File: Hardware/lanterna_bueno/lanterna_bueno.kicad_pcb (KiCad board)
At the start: 2 copper layers, 50 parts, among them J1 USB_B_Micro, Q1 BC807, Q2 2SK4075, Q3 2SK4075, Q4 2SK4075, Q5 2SK4075, SW1 SW_Push, SW2 SW_Push, SW3 SW_Push, U1 RT9193-33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

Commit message: add Mechanical DXF
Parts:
- moved DS1 67.9 mm to (88.9, 106.7)
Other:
- board outline added: 190.3 x 82.2 mm

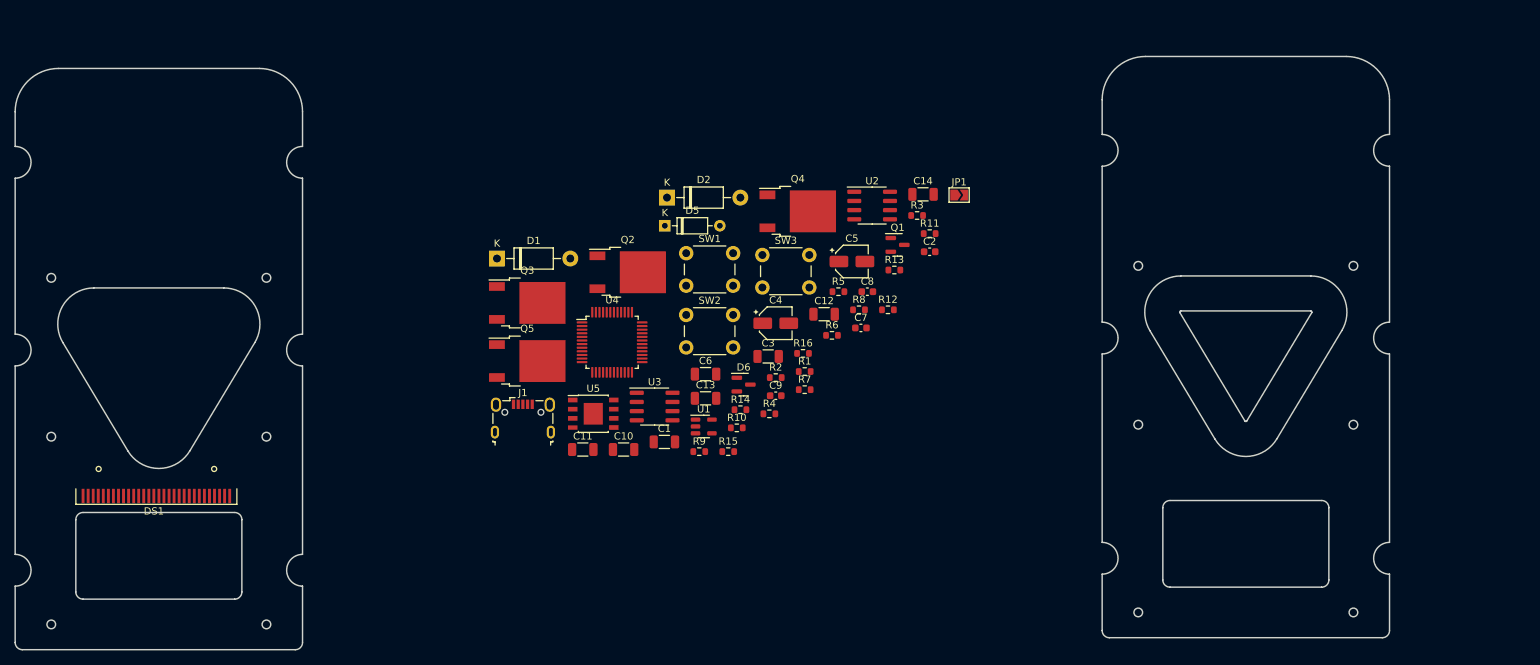
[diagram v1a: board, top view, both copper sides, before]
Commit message: Starting board, mounting holes OK
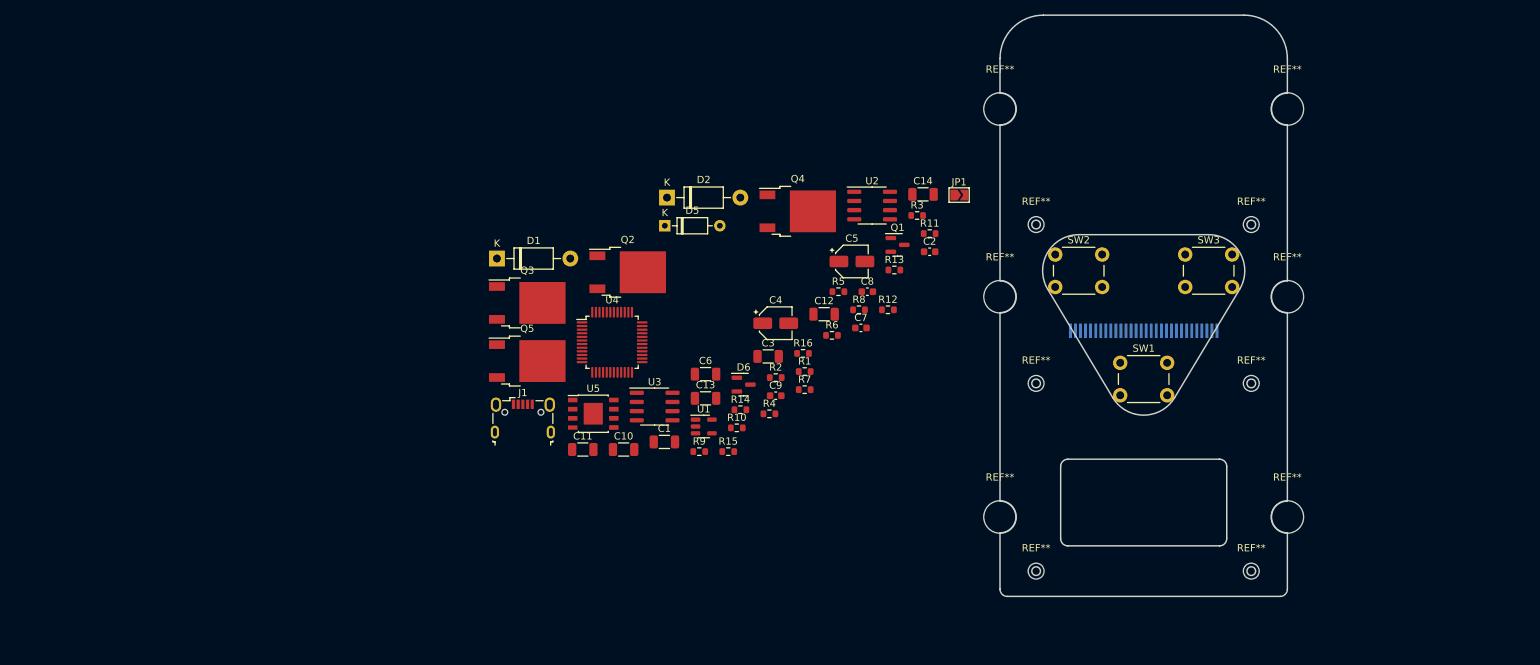
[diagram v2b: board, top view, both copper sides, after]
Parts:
- added REF**: MountingHole_2.2mm_M2, MountingHole:MountingHole_2.2mm_M2, F.Cu at (240.5, 69.1)
- added REF**: MountingHole_4.5mm, MountingHole:MountingHole_4.5mm, F.Cu at (205.7, 53.1)
- added REF**: MountingHole_2.2mm_M2, MountingHole:MountingHole_2.2mm_M2, F.Cu at (210.7, 117.1)
- added REF**: MountingHole_2.2mm_M2, MountingHole:MountingHole_2.2mm_M2, F.Cu at (240.5, 91.1)
- added REF**: MountingHole_4.5mm, MountingHole:MountingHole_4.5mm, F.Cu at (245.5, 53.1)
- added REF**: MountingHole_4.5mm, MountingHole:MountingHole_4.5mm, F.Cu at (205.7, 79.1)
- added REF**: MountingHole_2.2mm_M2, MountingHole:MountingHole_2.2mm_M2, F.Cu at (210.7, 69.1)
- added REF**: MountingHole_4.5mm, MountingHole:MountingHole_4.5mm, F.Cu at (205.7, 109.6)
- added REF**: MountingHole_2.2mm_M2, MountingHole:MountingHole_2.2mm_M2, F.Cu at (210.7, 91.1)
- added REF**: MountingHole_2.2mm_M2, MountingHole:MountingHole_2.2mm_M2, F.Cu at (240.5, 117.1)
- added REF**: MountingHole_4.5mm, MountingHole:MountingHole_4.5mm, F.Cu at (245.5, 109.6)
- added REF**: MountingHole_4.5mm, MountingHole:MountingHole_4.5mm, F.Cu at (245.5, 79.1)
- DS1: moved to B.Cu
- moved DS1 138.6 mm to (225.6, 83.8)
- moved SW1 62.0 mm to (222.4, 88.2)
- moved SW3 58.6 mm to (231.4, 73.2)
- moved SW2 51.8 mm to (213.4, 73.2)
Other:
- board size 190.3 x 82.2 mm -> 39.8 x 80.5 mm

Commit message: Flat do Oled posicionado
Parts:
- BTN +: renamed from SW2
- BTN -: renamed from SW3
- BTN M: renamed from SW1
- JP1, U4: moved to B.Cu
- moved U4 76.3 mm to (225.3, 64.0), turned to -45 degrees
- moved JP1 20.6 mm to (218.9, 56.6), turned to 45 degrees
- moved DS1 17.8 mm to (225.7, 101.6)
- moved BTN - 7.93 mm to (237.9, 77.7), turned to 180 degrees
- moved BTN + 7.90 mm to (219.9, 77.7), turned to 180 degrees
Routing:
- added copper zone on B.Cu, net GND
- added copper zone on F.Cu, net GND
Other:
- outline, holes or cut-outs redrawn

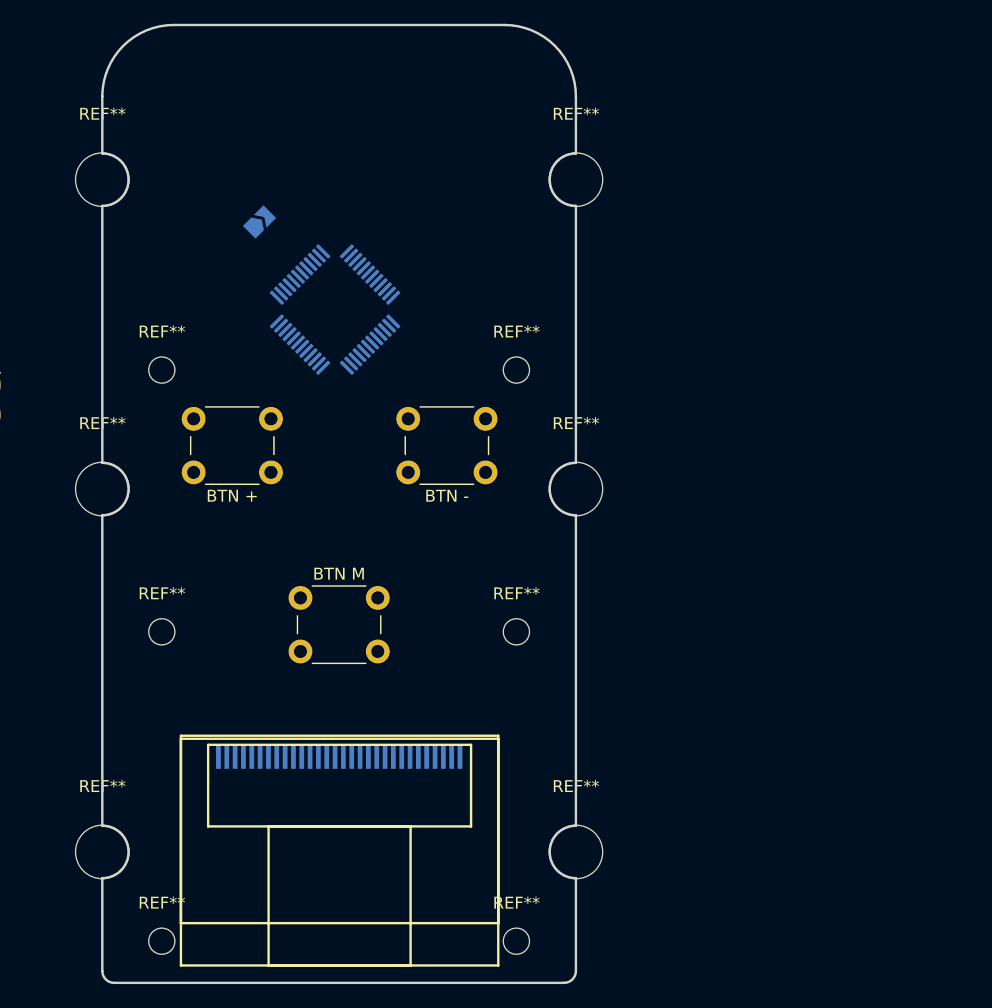
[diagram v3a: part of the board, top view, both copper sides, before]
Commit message: Adicionado PCB Carga e Board Profile corrigido
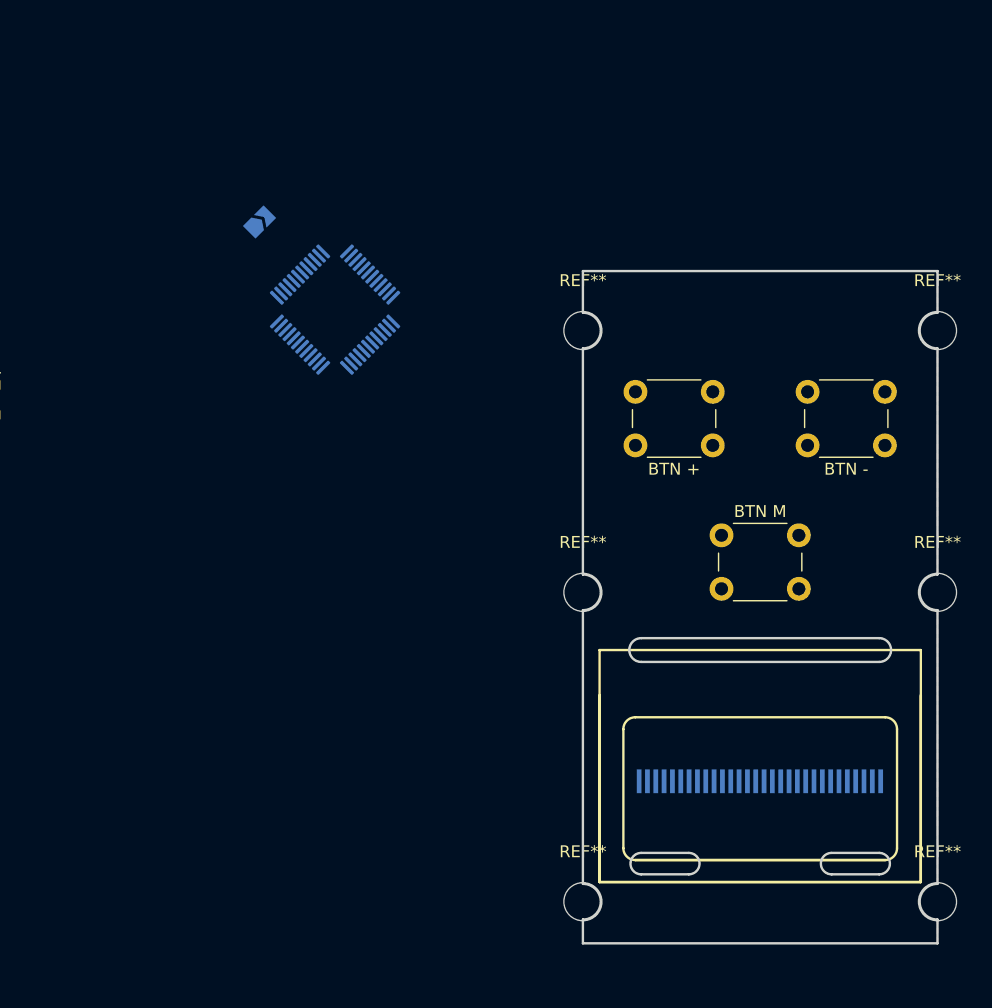
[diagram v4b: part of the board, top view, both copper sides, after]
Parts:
- removed the REF** at (240.5, 69.1)
- removed the REF** at (205.7, 53.1)
- removed the REF** at (210.7, 117.1)
- removed the REF** at (240.5, 91.1)
- removed the REF** at (245.5, 53.1)
- removed the REF** at (205.7, 79.1)
- removed the REF** at (210.7, 69.1)
- removed the REF** at (205.7, 109.6)
- removed the REF** at (210.7, 91.1)
- removed the REF** at (240.5, 117.1)
- removed the REF** at (245.5, 109.6)
- removed the REF** at (245.5, 79.1)
- added REF**: MountingHole_3.2mm_M3, MountingHole:MountingHole_3.2mm_M3, F.Cu at (246.1, 87.8)
- added REF**: MountingHole_3.2mm_M3, MountingHole:MountingHole_3.2mm_M3, F.Cu at (275.9, 113.8)
- added REF**: MountingHole_3.2mm_M3, MountingHole:MountingHole_3.2mm_M3, F.Cu at (246.1, 113.8)
- added REF**: MountingHole_3.2mm_M3, MountingHole:MountingHole_3.2mm_M3, F.Cu at (275.9, 87.8)
- added REF**: MountingHole_3.2mm_M3, MountingHole:MountingHole_3.2mm_M3, F.Cu at (246.1, 65.8)
- added REF**: MountingHole_3.2mm_M3, MountingHole:MountingHole_3.2mm_M3, F.Cu at (275.9, 65.8)
- moved BTN + 37.2 mm to (257.0, 75.4)
- moved BTN M 35.8 mm to (257.8, 83.0)
- moved DS1 35.4 mm to (261.0, 103.6), turned to 180 degrees
- moved BTN - 33.6 mm to (271.5, 75.4)
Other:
- board size 39.8 x 80.5 mm -> 29.8 x 56.5 mm

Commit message: building
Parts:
- removed C10: 1uF, Capacitor_SMD:C_1206_3216Metric
- removed C7: 100nF, Capacitor_SMD:C_0603_1608Metric
- removed D6: BAT54C, Package_TO_SOT_SMD:SOT-23
- removed JP1: SolderJumper_2_Open, Jumper:SolderJumper-2_P1.3mm_Open_TrianglePad1.0x1.5mm
- removed R8: 47K, Resistor_SMD:R_0603_1608Metric
- C12, C13: footprint Capacitor_SMD:C_1206_3216Metric -> Capacitor_SMD:C_0603_1608Metric
- D1, D2: footprint Diode_THT:D_DO-41_SOD81_P10.16mm_Horizontal -> Diode_SMD:D_SMA
- D5: footprint Diode_THT:D_DO-35_SOD27_P7.62mm_Horizontal -> Diode_SMD:D_SOD-123
- SW1: renamed from BTN M; footprint Button_Switch_THT:SW_PUSH_6mm -> Button_Switch_SMD:SW_Push_1P1T_NO_6x6mm_H9.5mm
- SW2: renamed from BTN +; footprint Button_Switch_THT:SW_PUSH_6mm -> Button_Switch_SMD:SW_Push_1P1T_NO_6x6mm_H9.5mm
- SW3: renamed from BTN -; footprint Button_Switch_THT:SW_PUSH_6mm -> Button_Switch_SMD:SW_Push_1P1T_NO_6x6mm_H9.5mm
- U2: moved to B.Cu
- U4: value STM32F103CBTx -> STM32F042K6Tx; footprint Package_QFP:LQFP-48_7x7mm_P0.5mm -> Package_QFP:LQFP-32_7x7mm_P0.8mm
- moved SW3 76.8 mm to (194.8, 80.6)
- moved SW2 76.8 mm to (180.4, 80.5)
- moved REF** 73.8 mm to (202.5, 121.1)
- moved REF** 73.8 mm to (202.5, 95.1)
- moved REF** 73.8 mm to (202.5, 73.1)
- moved DS1 73.8 mm to (187.6, 111.0)
- moved REF** 73.8 mm to (172.7, 95.1)
- moved REF** 73.8 mm to (172.7, 121.1)
- moved REF** 73.8 mm to (172.7, 73.1)
- moved SW1 70.8 mm to (187.6, 92.6)
- moved D5 53.3 mm to (189.7, 113.0), turned to 180 degrees
- moved Q4 50.4 mm to (148.0, 107.9), turned to -90 degrees
- moved U5 47.9 mm to (197.3, 93.4), turned to 90 degrees
- moved C14 45.7 mm to (181.0, 108.4)
- moved C11 44.4 mm to (189.7, 115.3)
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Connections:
- U4 pad 1: VBAT -> +3V3
- U4 pad 10: BAT_MON -> unconnected-(U4-Pad10)
- U4 pad 12: unconnected-(U4-Pad12) -> PWM_LED_SUPH
- U4 pad 13: unconnected-(U4-Pad13) -> PWM_LED_SUPL
- U4 pad 14: unconnected-(U4-Pad14) -> PWM_LED_INFH
- U4 pad 15: unconnected-(U4-Pad15) -> PWM_LED_INFL
- U4 pad 16: PWM_LED_SUPH -> GND
- U4 pad 17: PWM_LED_SUPL -> +3V3
- U4 pad 18: PWM_LED_INFH -> unconnected-(U4-Pad18)
- U4 pad 19: PWM_LED_INFL -> unconnected-(U4-Pad19)
- U4 pad 2: unconnected-(U4-Pad2) -> LCD_SDA
- U4 pad 23: GND -> unconnected-(U4-Pad23)
- U4 pad 24: +3V3 -> unconnected-(U4-Pad24)
- U4 pad 25: BUT_MINUS -> unconnected-(U4-Pad25)
- U4 pad 26: BUT_PLUS -> BUT_MINUS
- U4 pad 27: BUT_MENU -> BUT_PLUS
- U4 pad 28: POWER_CMD -> BUT_MENU
- U4 pad 29: unconnected-(U4-Pad29) -> POWER_CMD
- U4 pad 3: unconnected-(U4-Pad3) -> LCD_SCL
- U4 pad 32: unconnected-(U4-Pad32) -> GND
- U4 pad 4: unconnected-(U4-Pad4) -> Net-(R9-Pad2)
- U4 pad 5: unconnected-(U4-Pad5) -> +3V3
- U4 pad 6: unconnected-(U4-Pad6) -> BAT_MON
- U4 pad 7: Net-(R9-Pad2) -> unconnected-(U4-Pad7)
- U4 pad 8: GND -> unconnected-(U4-Pad8)
- U4 pad 9: +3V3 -> unconnected-(U4-Pad9)
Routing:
- added copper zone on B.Cu, net (none)
- added copper zone on F.Cu, net (none)
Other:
- board size 29.8 x 56.5 mm -> 75 x 56.5 mm

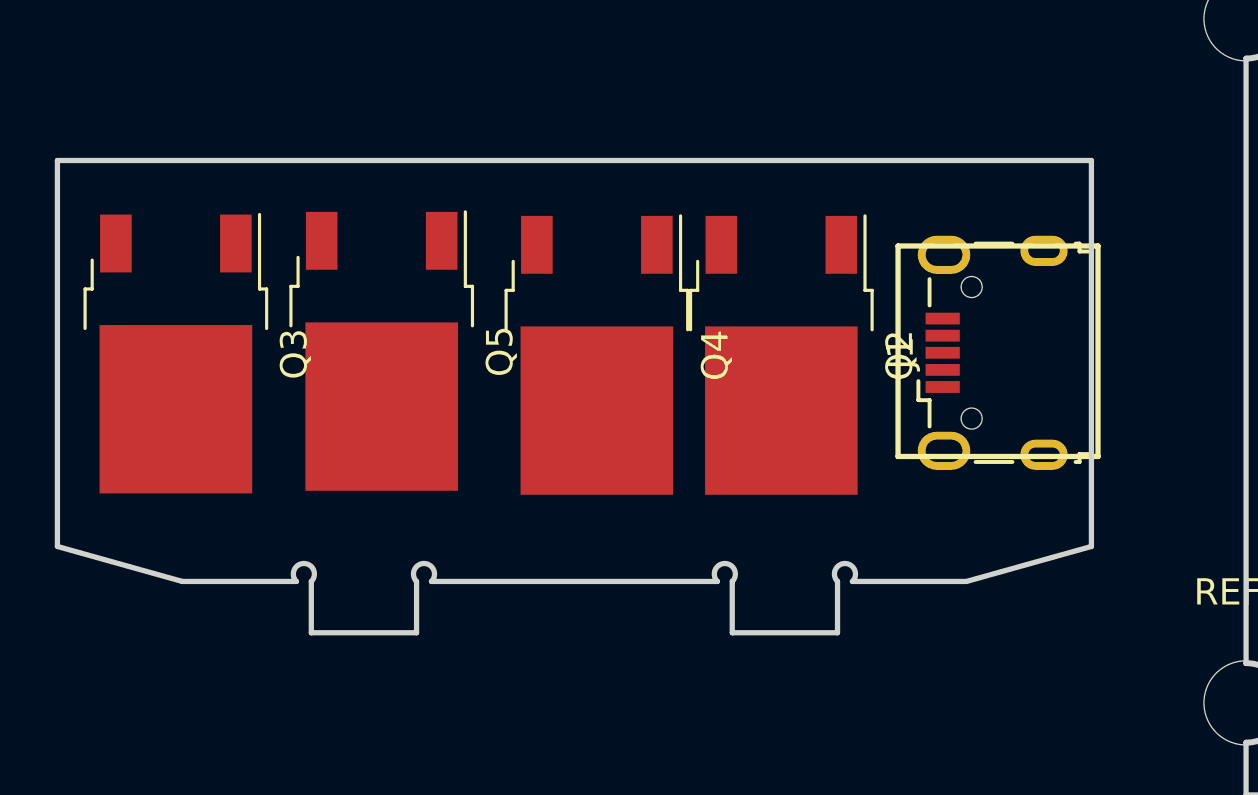
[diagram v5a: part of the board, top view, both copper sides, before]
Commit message: Usb PCB Chamfer
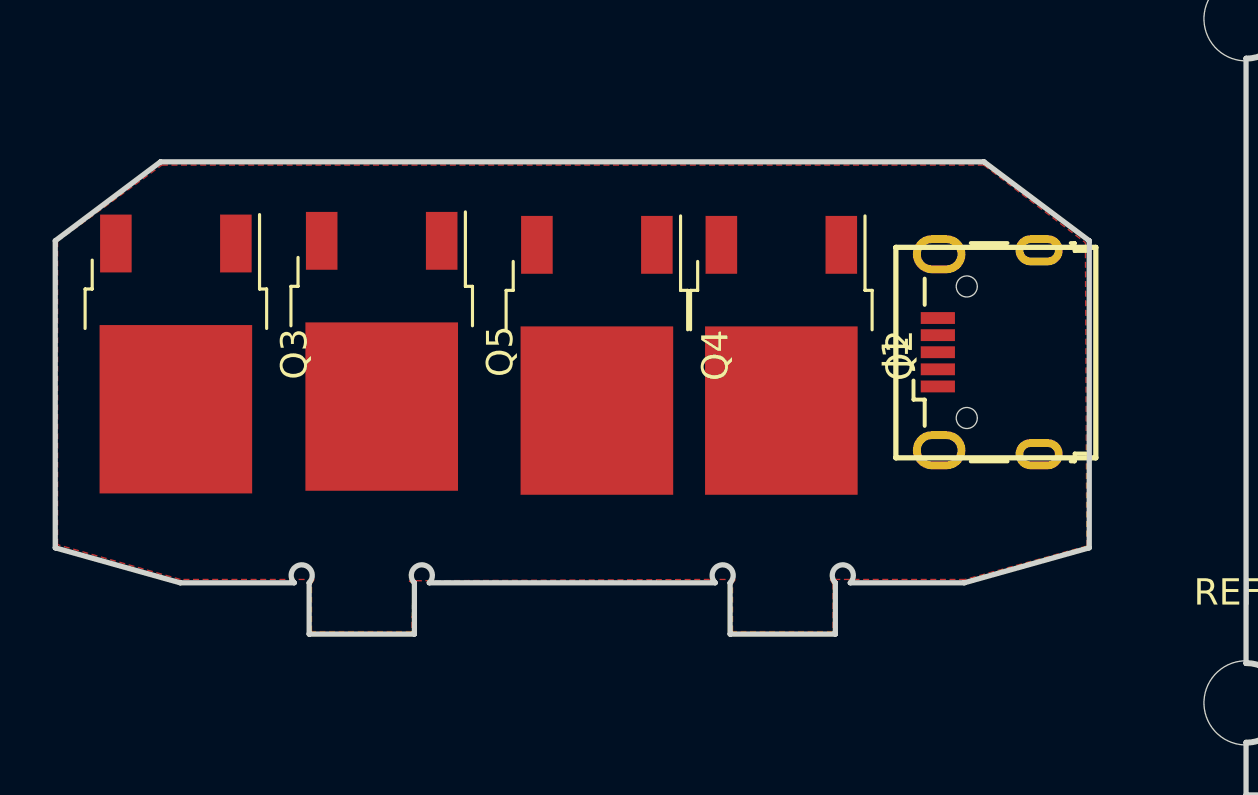
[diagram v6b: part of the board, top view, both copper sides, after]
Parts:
- moved J1 0.19 mm to (162.9, 107.8)
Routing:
- removed copper zone on B.Cu, net (none)
- removed copper zone on F.Cu, net (none)
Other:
- board size 75 x 56.5 mm -> 75.1 x 56.5 mm
